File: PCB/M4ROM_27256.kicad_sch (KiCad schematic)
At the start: 7 parts, among them J1 32Kx8_mask_rom_socket, J2 4ROM_prog_female, SW1 CUS-14TB, U1 29F010

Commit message: MPN boms, centroids, and chip unavailability notes
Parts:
- C1: MPN (none) -> CL21B105KBFNNNE
- D1: MPN (none) -> BAV70S,115
- J1, J2: now left out of the parts list
- RA1: MPN (none) -> YC164-JR-07200KL
- SW1: MPN (none) -> CUS-14TB
- U1: MPN (none) -> SST39SF010A-70-4C-WHE
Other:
- note added: "Footprint compatible with 128Kx8 to 512Kx8, though only 128K is used. 5V. 8x14mm TSOP-I-32 Examples: SST39SF0x0x-xx-xx-WHx ex: SST39SF010A-70-4C-WHE SST39SF020A SST39SF040 GLS29EE0x0-xx-xx-WHx ex: GLS29EE010-70-4C-WHE Feb 2025: no known active compatible parts"
- note removed: "SST39SF010A"
- note removed: "U1: Any 29F010, 29F020, or 29F040 compatible may be installed, but only 128k is used, so ideal is 29F010. ex: SST39SF010A RA1: YC164-JR-07200KL D1: Any 2-pair common-cathode 6TSSOP. ex: BAV70S, BAT54CDW"
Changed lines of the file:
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@@
 	(title_block
 		(title "M4ROM 27256")
-		(date "2023-12-31")
-		(rev "004")
+		(date "2025-02-21")
+		(rev "005")
 		(company "Brian K. White b.kenyon.w@gmail.com")
 		(comment 1 "CC-BY-SA")
@@
 		)
 	)
-	(text "U1: Any 29F010, 29F020, or 29F040 compatible may be installed,\nbut only 128k is used, so ideal is 29F010. ex: SST39SF010A\n\nRA1: YC164-JR-07200KL\n\nD1: Any 2-pair common-cathode 6TSSOP. ex: BAV70S, BAT54CDW\n"
+	(text "Footprint compatible with 128Kx8 to 512Kx8,\nthough only 128K is used. 5V. 8x14mm TSOP-I-32\nExamples:\nSST39SF0x0x-xx-xx-WHx ex: SST39SF010A-70-4C-WHE SST39SF020A SST39SF040\nGLS29EE0x0-xx-xx-WHx ex: GLS29EE010-70-4C-WHE\nFeb 2025: no known active compatible parts\n"
 		(exclude_from_sim no)
-		(at 180.34 161.29 0)
+		(at 119.888 49.53 0)
 		(effects
 			(font
@@
 		)
 	)
-	(text "SST39SF010A"
-		(exclude_from_sim no)
-		(at 146.05 57.15 0)
-		(effects
-			(font
-				(size 1.27 1.27)
-			)
-			(justify left bottom)
-		)
-	)
 	(text "BANK SELECT"
 		(exclude_from_sim no)
@@
 			)
 		)
-		(property "Description" ""
+		(property "Description" "IC FLASH 128K-512Kx8 5V PARALLEL 32TSOP 8x14mm"
+			(at 152.4 88.9 0)
+			(effects
+				(font
+					(size 1.27 1.27)
+				)
+				(hide yes)
+			)
+		)
+		(property "MPN" "SST39SF010A-70-4C-WHE"
 			(at 152.4 88.9 0)
 			(effects
@@
 		(unit 1)
 		(exclude_from_sim no)
-		(in_bom yes)
+		(in_bom no)
 		(on_board yes)
 		(dnp no)
@@
 			)
 		)
-		(property "Datasheet" "http://www.vishay.com/docs/31509/csc.pdf"
+		(property "Datasheet" "datasheets/YC164.pdf"
 			(at 190.5 72.39 90)
 			(effects
@@
 			)
 		)
-		(property "Description" ""
+		(property "Description" "RES ARRAY 4 x 200K isolated 1206 4x0612 convex"
+			(at 190.5 72.39 0)
+			(effects
+				(font
+					(size 1.27 1.27)
+				)
+				(hide yes)
+			)
+		)
+		(property "MPN" "YC164-JR-07200KL"
 			(at 190.5 72.39 0)
 			(effects
@@
 			)
 		)
-		(property "Datasheet" "~"
+		(property "Datasheet" "datasheets/cus.pdf"
 			(at 60.96 160.02 0)
 			(effects
@@
 			)
 		)
-		(property "Description" ""
+		(property "Description" "CUS-14TB Switch, 4 position, single pole 4 throw, 4 position switch, SP4T"
+			(at 60.96 160.02 0)
+			(effects
+				(font
+					(size 1.27 1.27)
+				)
+				(hide yes)
+			)
+		)
+		(property "MPN" "CUS-14TB"
 			(at 60.96 160.02 0)
 			(effects
@@
 			)
 		)
-		(property "Description" ""
+		(property "Description" "BAV70S 100V 250mA high-speed switching diodes, dual common cathode, SOT-363"
+			(at 85.09 158.75 0)
+			(effects
+				(font
+					(size 1.27 1.27)
+				)
+				(hide yes)
+			)
+		)
+		(property "MPN" "BAV70S,115"
 			(at 85.09 158.75 0)
 			(effects
@@
 			)
 		)
-		(property "Description" ""
+		(property "Description" "BAV70S 100V 250mA high-speed switching diodes, dual common cathode, SOT-363"
+			(at 101.6 161.29 0)
+			(effects
+				(font
+					(size 1.27 1.27)
+				)
+				(hide yes)
+			)
+		)
+		(property "MPN" "BAV70S,115"
 			(at 101.6 161.29 0)
 			(effects
@@
 			)
 		)
-		(property "Datasheet" "~"
+		(property "Datasheet" "datasheets/CL21B105KBFNNNE.pdf"
 			(at 127 63.5 0)
 			(effects
@@
 			)
 		)
-		(property "Description" ""
+		(property "Description" "CAP CER 1UF 16V+ 0805"
+			(at 127 63.5 0)
+			(effects
+				(font
+					(size 1.27 1.27)
+				)
+				(hide yes)
+			)
+		)
+		(property "MPN" "CL21B105KBFNNNE"
 			(at 127 63.5 0)
 			(effects
@@
 			)
 		)
-		(property "Datasheet" "http://www.vishay.com/docs/31509/csc.pdf"
+		(property "Datasheet" "datasheets/YC164.pdf"
 			(at 83.82 185.42 90)
 			(effects
@@
 			)
 		)
-		(property "Description" ""
+		(property "Description" "RES ARRAY 4 x 200K isolated 1206 4x0612 convex"
+			(at 83.82 185.42 0)
+			(effects
+				(font
+					(size 1.27 1.27)
+				)
+				(hide yes)
+			)
+		)
+		(property "MPN" "YC164-JR-07200KL"
 			(at 83.82 185.42 0)
 			(effects
@@
 		(unit 1)
 		(exclude_from_sim no)
-		(in_bom yes)
+		(in_bom no)
 		(on_board yes)
 		(dnp no)
@@
 			)
 		)
-		(property "Datasheet" "http://www.vishay.com/docs/31509/csc.pdf"
+		(property "Datasheet" "datasheets/YC164.pdf"
 			(at 81.28 152.4 90)
 			(effects
@@
 			)
 		)
-		(property "Description" ""
+		(property "Description" "RES ARRAY 4 x 200K isolated 1206 4x0612 convex"
+			(at 81.28 152.4 0)
+			(effects
+				(font
+					(size 1.27 1.27)
+				)
+				(hide yes)
+			)
+		)
+		(property "MPN" "YC164-JR-07200KL"
 			(at 81.28 152.4 0)
 			(effects
@@
 			)
 		)
-		(property "Datasheet" "http://www.vishay.com/docs/31509/csc.pdf"
+		(property "Datasheet" "datasheets/YC164.pdf"
 			(at 97.79 154.94 90)
 			(effects
@@
 			)
 		)
-		(property "Description" ""
+		(property "Description" "RES ARRAY 4 x 200K isolated 1206 4x0612 convex"
+			(at 97.79 154.94 0)
+			(effects
+				(font
+					(size 1.27 1.27)
+				)
+				(hide yes)
+			)
+		)
+		(property "MPN" "YC164-JR-07200KL"
 			(at 97.79 154.94 0)
 			(effects

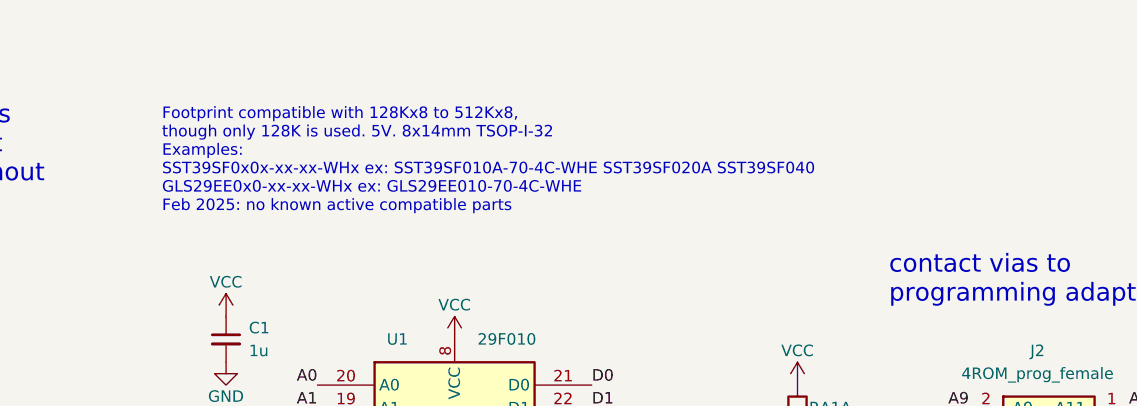
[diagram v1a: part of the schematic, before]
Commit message: new flash part number
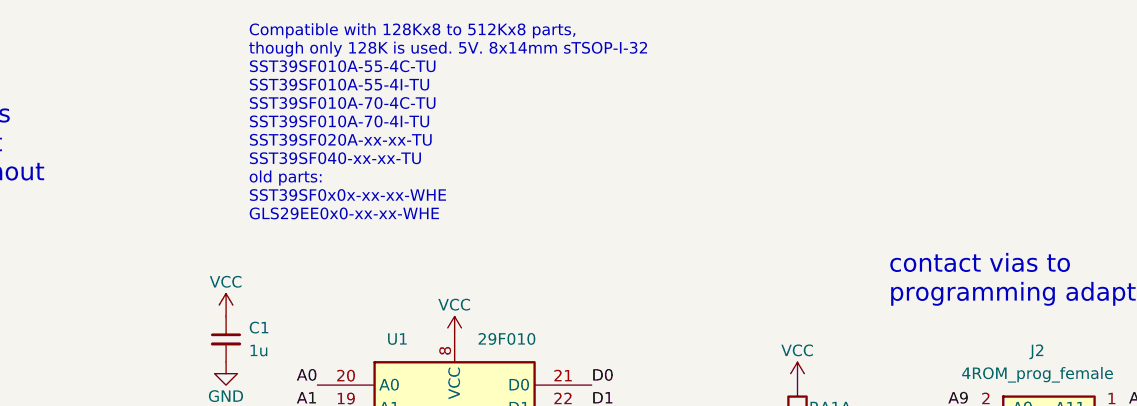
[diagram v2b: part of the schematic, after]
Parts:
- U1: MPN SST39SF010A-70-4C-WHE -> SST39SF010A-70-4C-TU
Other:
- note added: "Compatible with 128Kx8 to 512Kx8 parts, though only 128K is used. 5V. 8x14mm sTSOP-I-32 SST39SF010A-55-4C-TU SST39SF010A-55-4I-TU SST39SF010A-70-4C-TU SST39SF010A-70-4I-TU SST39SF020A-xx-xx-TU SST39SF040-xx-xx-TU old parts: SST39SF0x0x-xx-xx-WHE GLS29EE0x0-xx-xx-WHE"
- note removed: "Footprint compatible with 128Kx8 to 512Kx8, though only 128K is used. 5V. 8x14mm TSOP-I-32 Examples: SST39SF0x0x-xx-xx-WHx ex: SST39SF010A-70-4C-WHE SST39SF020A SST39SF040 GLS29EE0x0-xx-xx-WHx ex: GLS29EE010-70-4C-WHE Feb 2025: no known active compatible parts"
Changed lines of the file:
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@@
 		)
 	)
-	(text "Footprint compatible with 128Kx8 to 512Kx8,\nthough only 128K is used. 5V. 8x14mm TSOP-I-32\nExamples:\nSST39SF0x0x-xx-xx-WHx ex: SST39SF010A-70-4C-WHE SST39SF020A SST39SF040\nGLS29EE0x0-xx-xx-WHx ex: GLS29EE010-70-4C-WHE\nFeb 2025: no known active compatible parts\n"
+	(text "Compatible with 128Kx8 to 512Kx8 parts,\nthough only 128K is used. 5V. 8x14mm sTSOP-I-32\nSST39SF010A-55-4C-TU\nSST39SF010A-55-4I-TU\nSST39SF010A-70-4C-TU\nSST39SF010A-70-4I-TU\nSST39SF020A-xx-xx-TU\nSST39SF040-xx-xx-TU\nold parts:\nSST39SF0x0x-xx-xx-WHE\nGLS29EE0x0-xx-xx-WHE"
 		(exclude_from_sim no)
-		(at 119.888 49.53 0)
+		(at 129.54 50.546 0)
 		(effects
 			(font
@@
 			)
 		)
-		(property "MPN" "SST39SF010A-70-4C-WHE"
+		(property "MPN" "SST39SF010A-70-4C-TU"
 			(at 152.4 88.9 0)
 			(effects
